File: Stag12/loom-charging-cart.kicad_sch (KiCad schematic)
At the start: 18 parts, among them J1 MAINS 16A, J2 CAN_S, K1 Relay_DPST-NO, SW1 E-Stop, SW11 SW_DPST, SW2 Latching Reset, SW3 Close AIRs

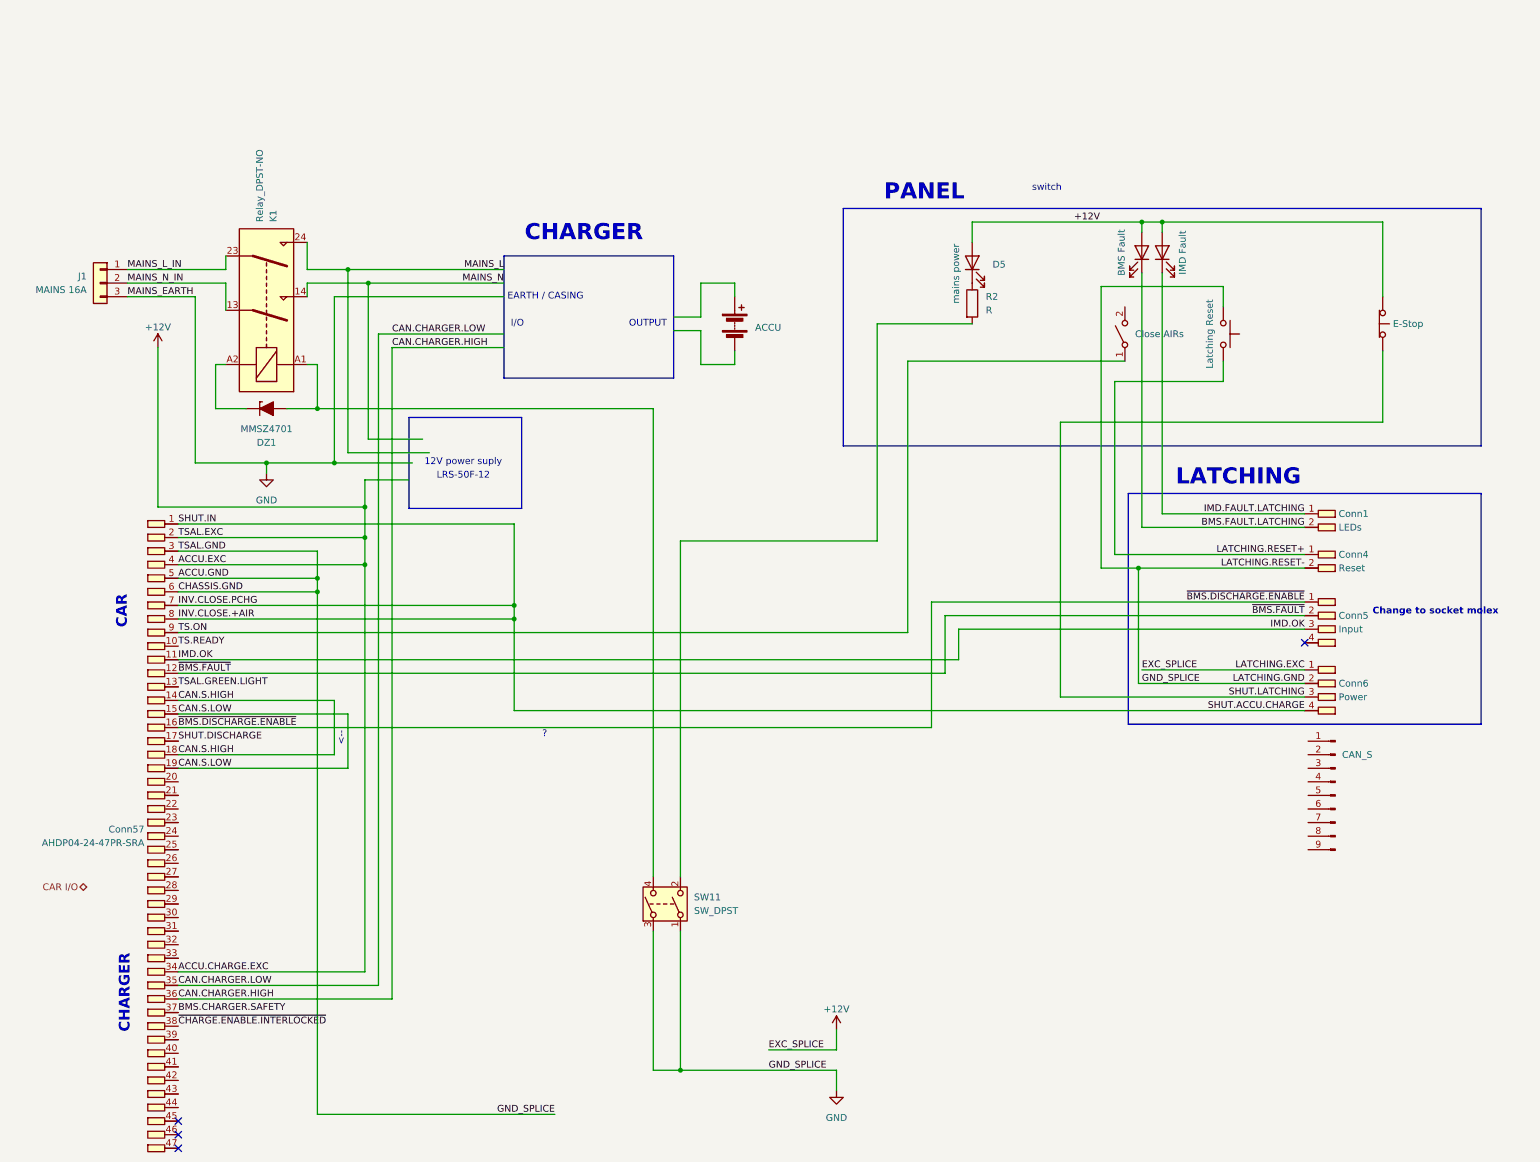
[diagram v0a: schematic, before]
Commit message: moved swiches to front panel
idk if this is right but i did it sooooo
yeah
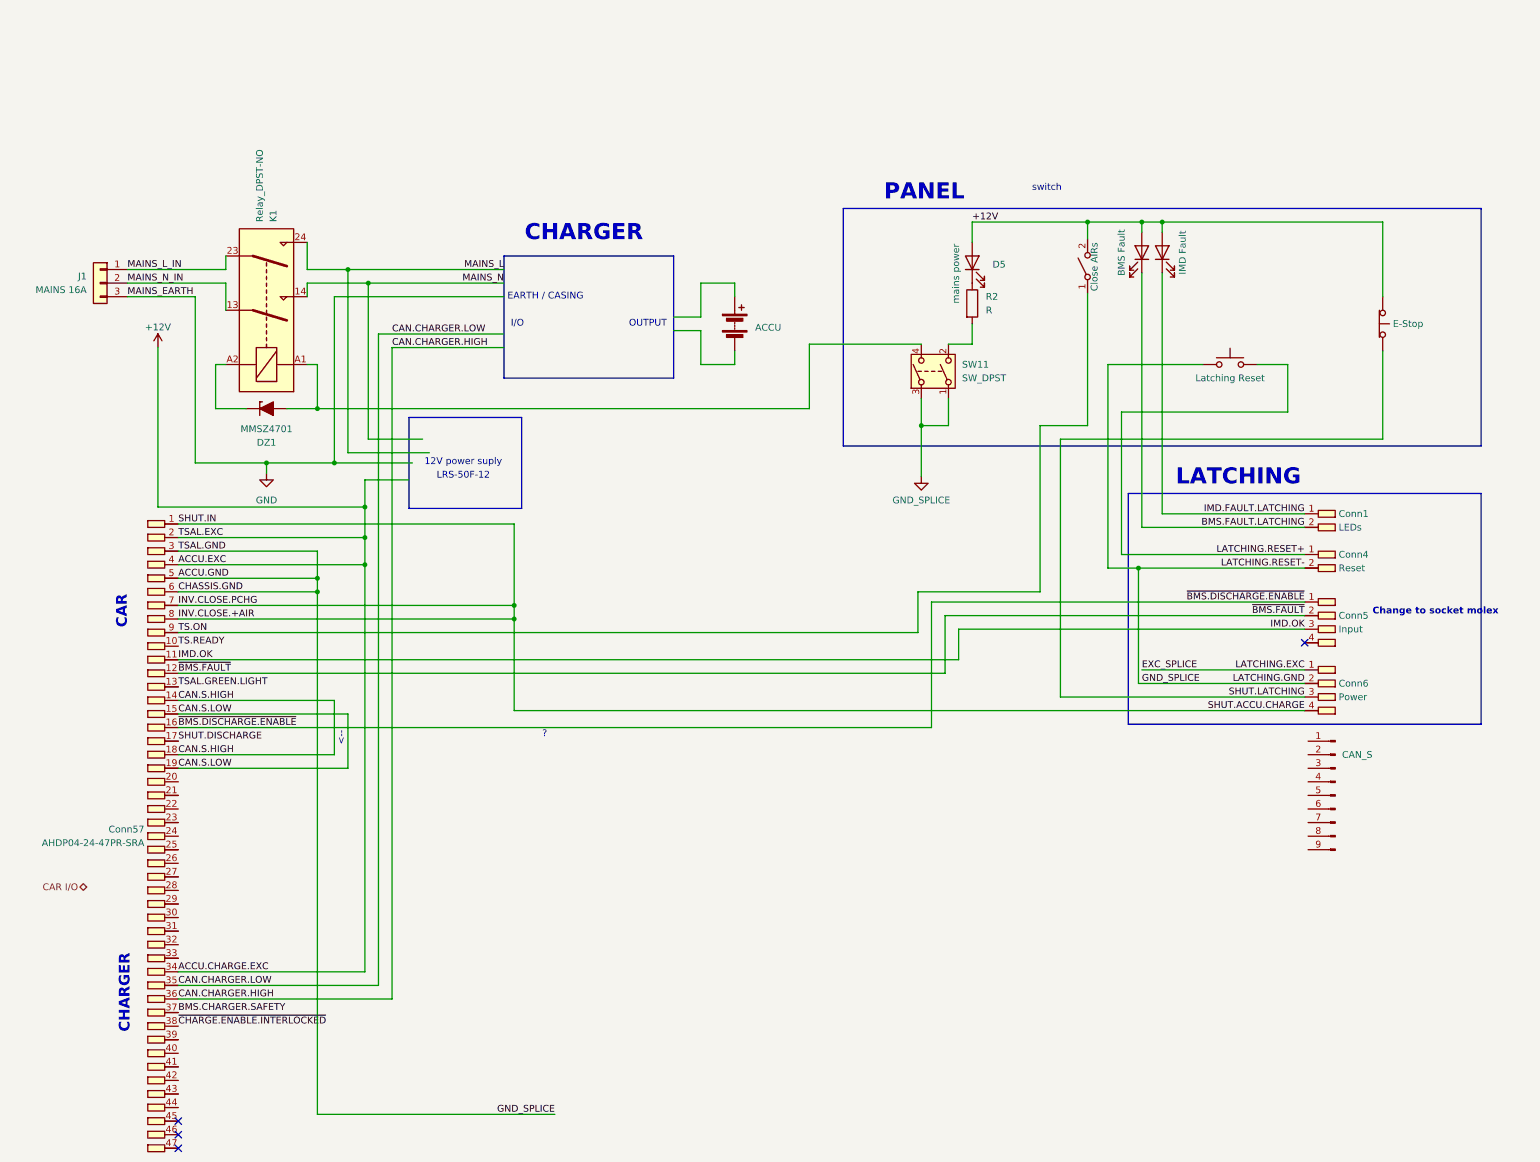
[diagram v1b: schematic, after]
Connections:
- net +12V: now also SW3.2 (B); no longer Conn6.1
- net GND: no longer Conn4.2, Conn57.3, Conn57.5, Conn57.6, Conn6.2, SW11.1, SW11.3, SW2.1
- new net EXC_SPLICE: Conn6.1
- new net GND_SPLICE: Conn4.2, Conn57.3, Conn57.5, Conn57.6, Conn6.2, SW11.1, SW11.3, SW2.1
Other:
- moved on the sheet: SW11

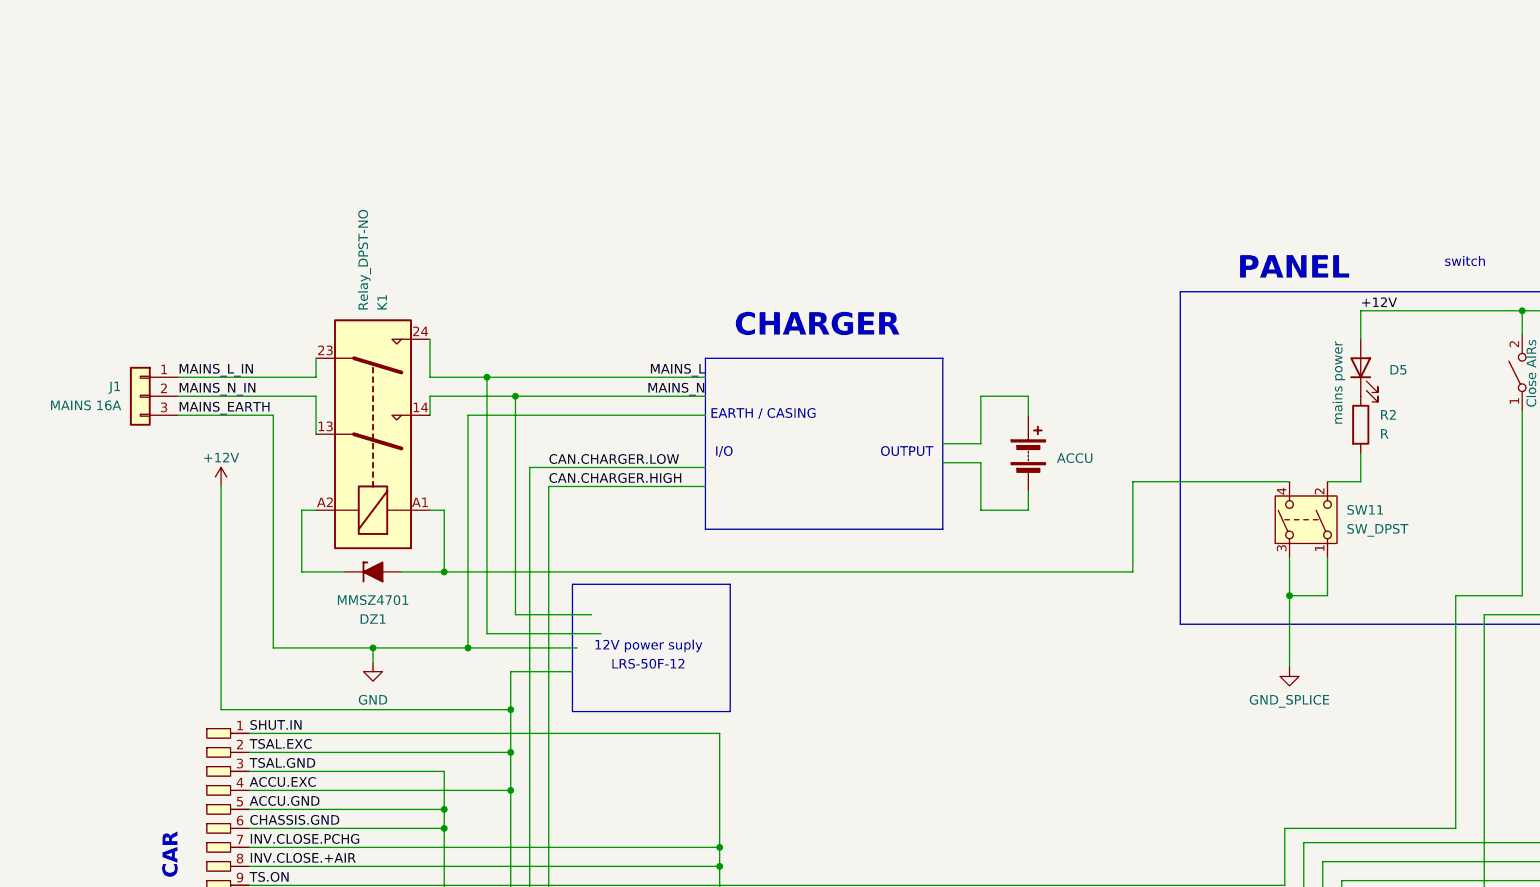
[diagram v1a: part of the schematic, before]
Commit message: Started rear loom
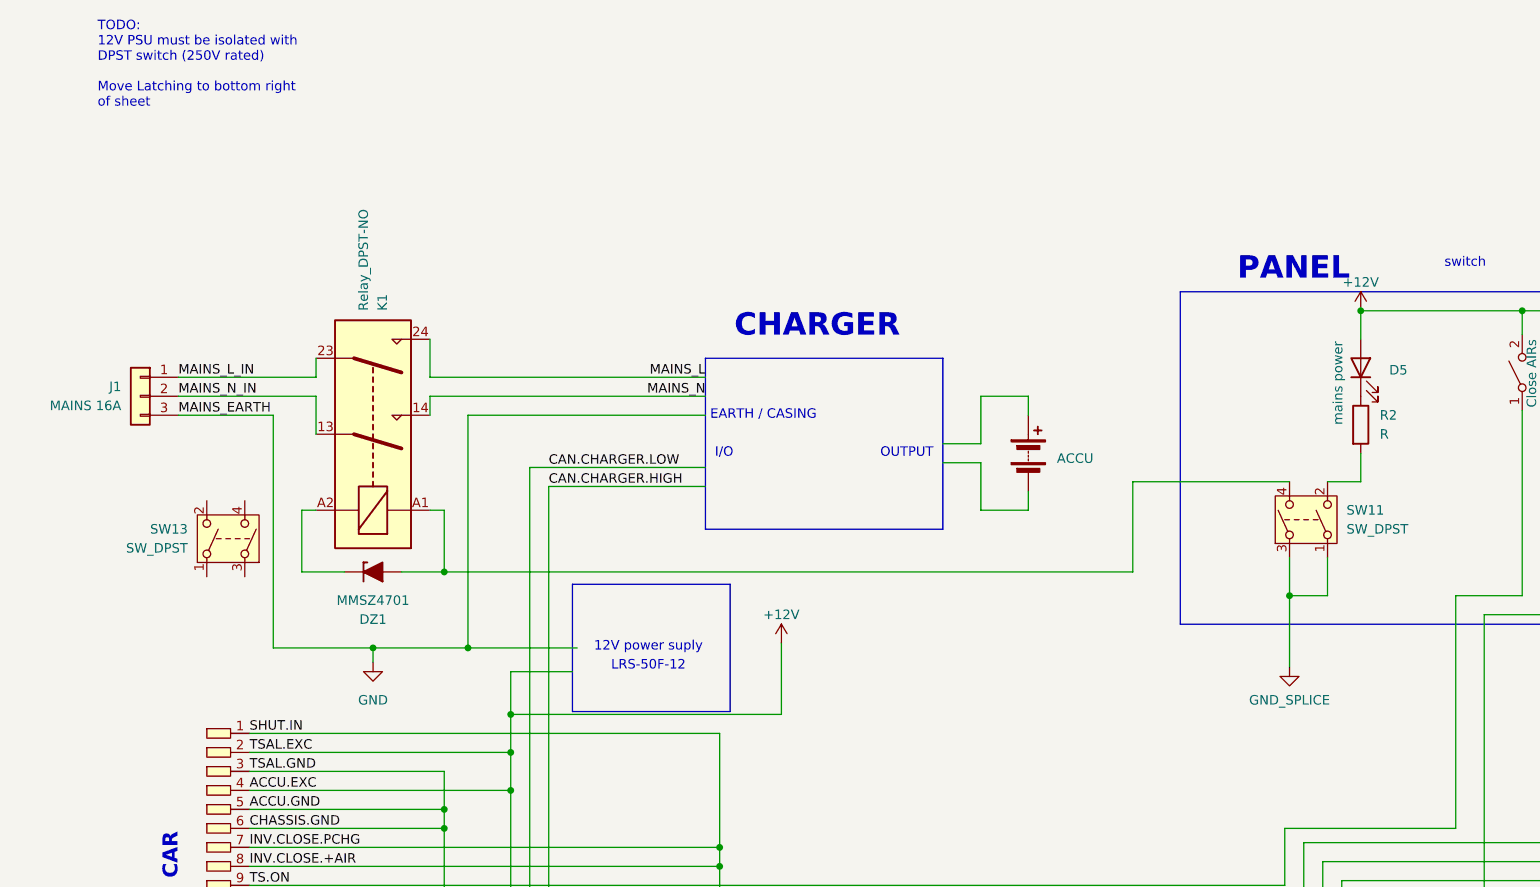
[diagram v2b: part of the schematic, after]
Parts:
- added SW13: SW_DPST, symbol Switch:SW_DPST
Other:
- note added: "TODO: 12V PSU must be isolated with DPST switch (250V rated) Move Latching to bottom right of sheet"

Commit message: Charging cart pogress
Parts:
- removed SW13: SW_DPST, symbol Switch:SW_DPST
- added SW14: SW_DPST, symbol Switch:SW_DPST
- J1: value MAINS 16A -> 523-2CMA193122R1000
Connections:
- net GND: now also SW11.1, SW11.3
- net MAINS_L: now also SW14.3
- net MAINS_N: now also SW14.1
- net GND_SPLICE renamed ACCU.GND
- net ACCU.GND: no longer SW11.1, SW11.3
- no-connect marks 4 -> 6
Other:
- moved on the sheet: Conn1, Conn4, Conn5, Conn6
